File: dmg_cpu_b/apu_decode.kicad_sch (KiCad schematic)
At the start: 67 parts

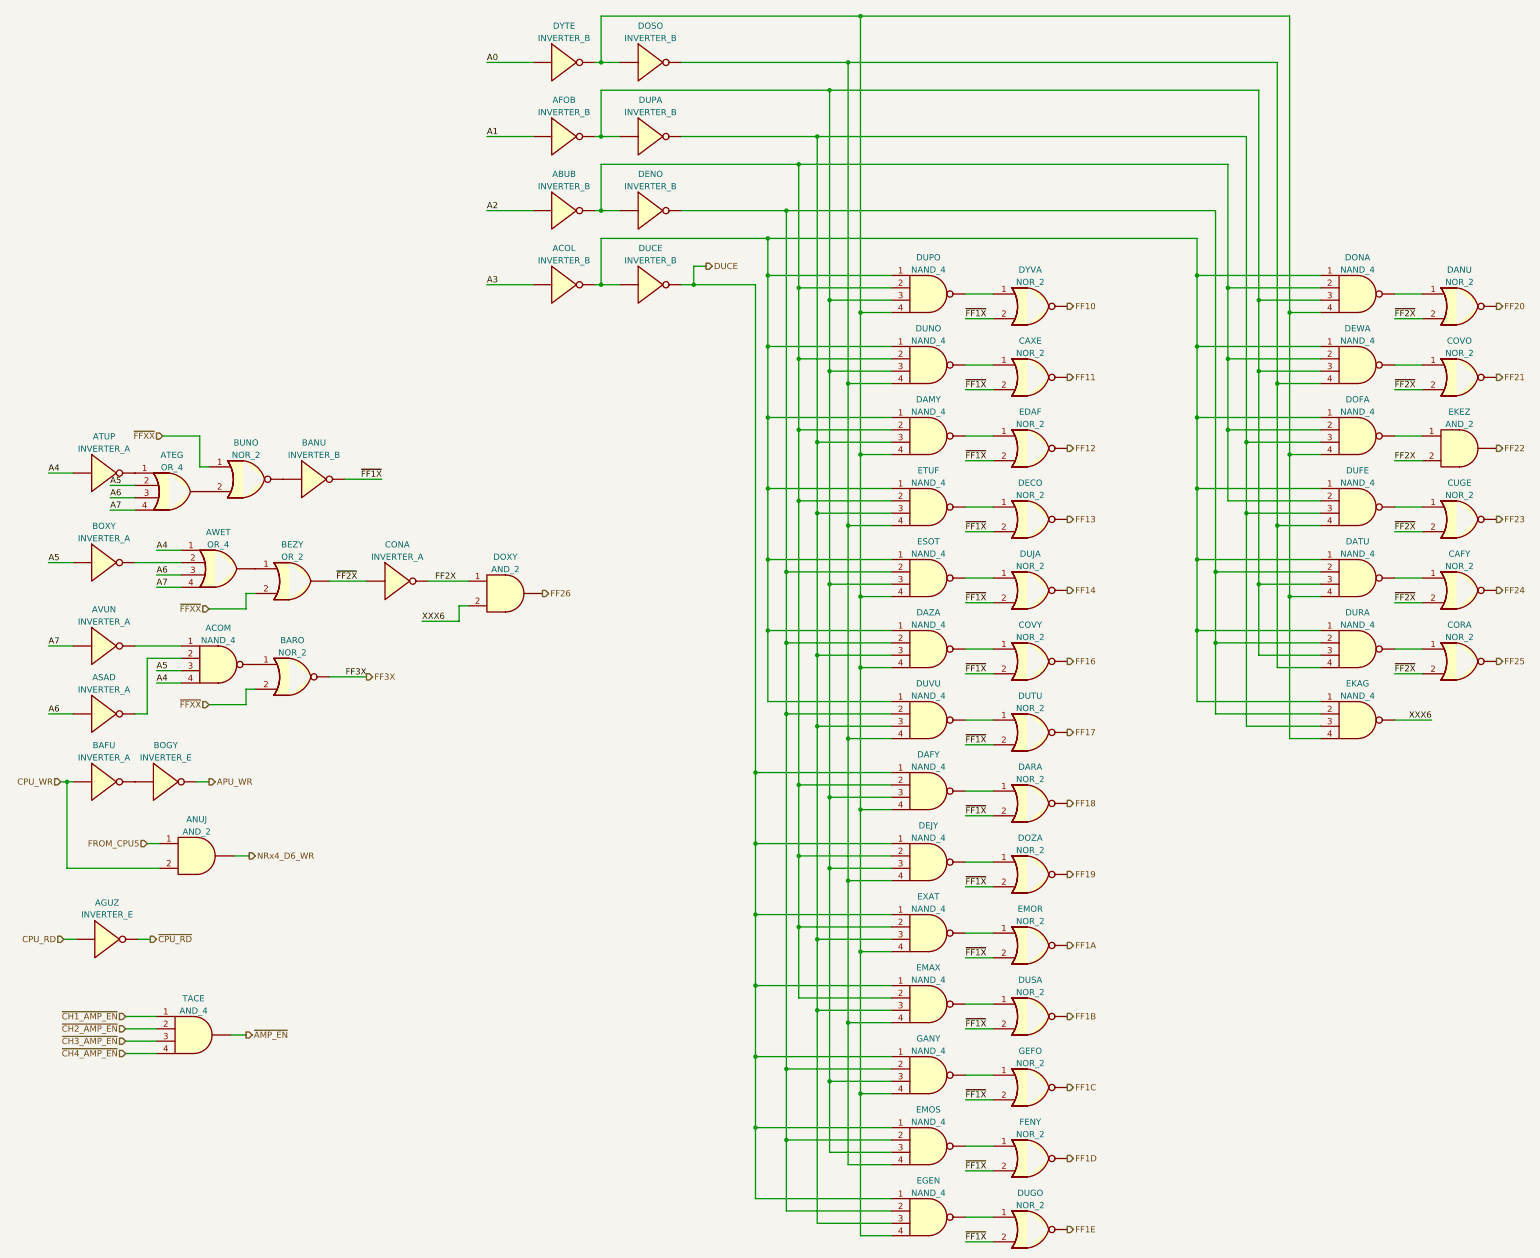
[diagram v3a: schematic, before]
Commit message: Fixes made from issues, channel 4 sheet aded and tidy up of hierarchical APU sheet. Small fixes done here and there when doing ERC.
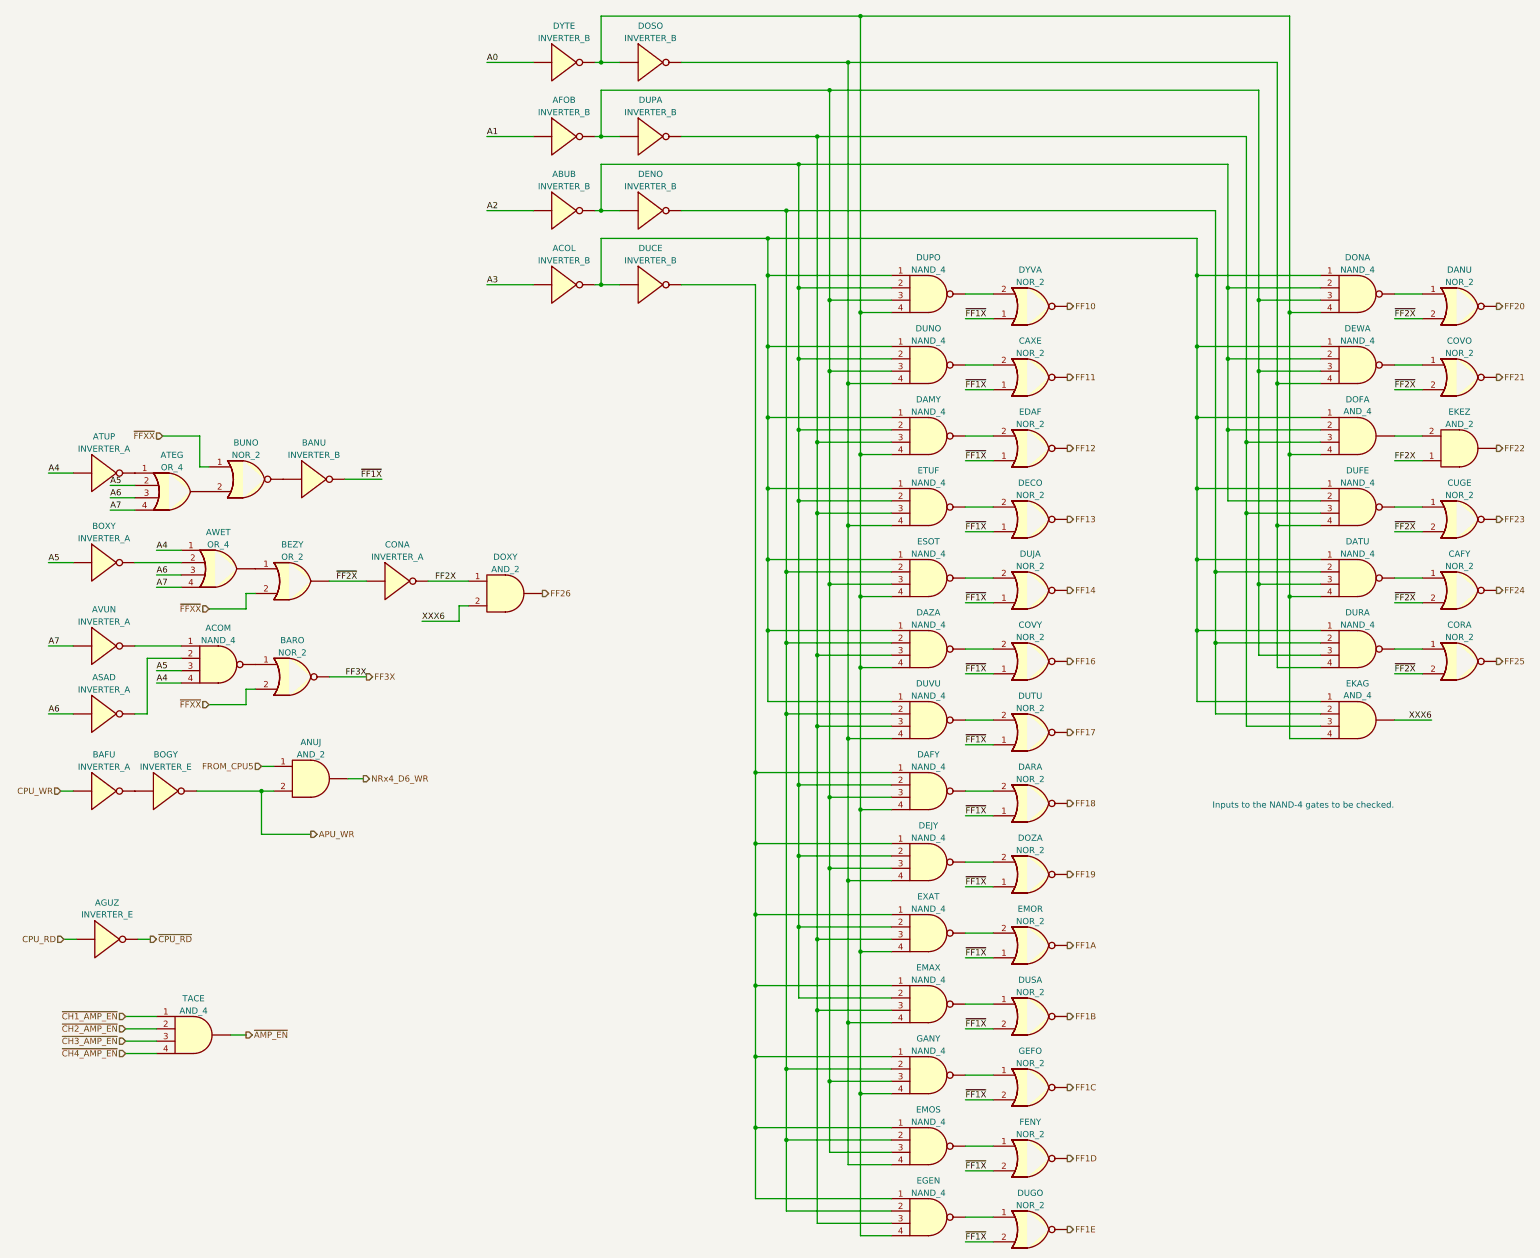
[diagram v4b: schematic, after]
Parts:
- DOFA, EKAG: value NAND_4 -> AND_4; symbol DMG_CPU_Cells:NAND_4 -> DMG_CPU_Cells:AND_4
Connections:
- net APU_WR: now also ANUJ.2
- net CPU_WR: no longer ANUJ.2
- net FF2X: now also EKEZ.1; no longer EKEZ.2
- net ~{FF1X}: now also CAXE.1, COVY.1, DARA.1, DECO.1, DOZA.1, DUJA.1, DUTU.1, DYVA.1, EDAF.1, EMOR.1; no longer CAXE.2, COVY.2, DARA.2, DECO.2, DOZA.2, DUJA.2, DUTU.2, DYVA.2, EDAF.2, EMOR.2
- net at DUVU.5: now also DUTU.2; no longer DUTU.1
- net at DUPO.5: now also DYVA.2; no longer DYVA.1
- net at ETUF.5: now also DECO.2; no longer DECO.1
- net at DAFY.5: now also DARA.2; no longer DARA.1
- net at DAZA.5: now also COVY.2; no longer COVY.1
- net at DOFA.5: now also EKEZ.2; no longer EKEZ.1
- net at EXAT.5: now also EMOR.2; no longer EMOR.1
- net at DAMY.5: now also EDAF.2; no longer EDAF.1
- net at DEJY.5: now also DOZA.2; no longer DOZA.1
- net at DUNO.5: now also CAXE.2; no longer CAXE.1
- net at ESOT.5: now also DUJA.2; no longer DUJA.1
- net DUCE: no longer names the net of DAFY.1, DEJY.1, DUCE.2, EGEN.1, EMAX.1, EMOS.1, EXAT.1, GANY.1
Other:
- note added: "Inputs to the NAND-4 gates to be checked."
- moved on the sheet: ANUJ, BAFU, BOGY

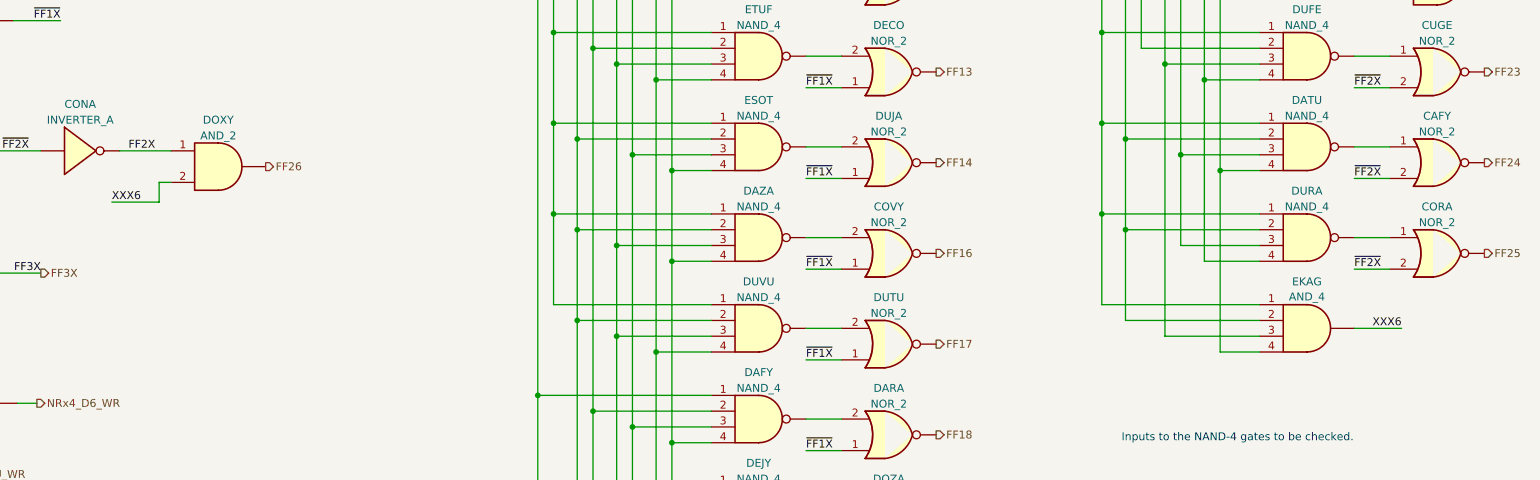
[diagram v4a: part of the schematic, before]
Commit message: DOXY moved for consistency.
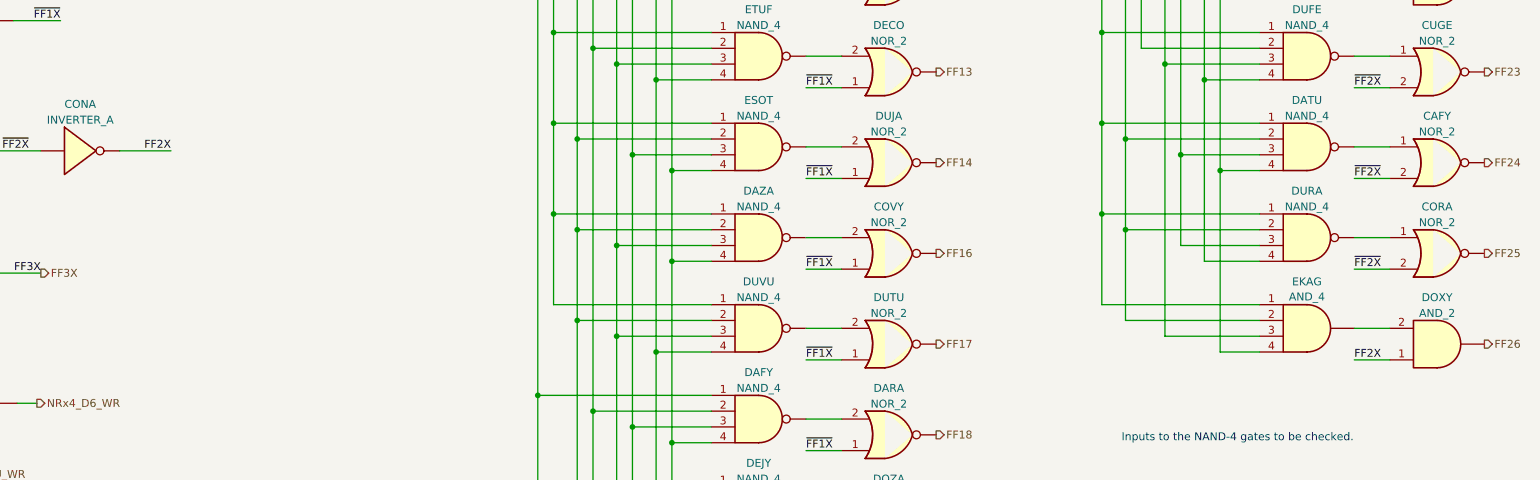
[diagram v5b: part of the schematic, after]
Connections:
- net XXX6: no longer names the net of DOXY.2, EKAG.5
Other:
- moved on the sheet: DOXY
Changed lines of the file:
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@@
     (stroke (width 0) (type default) (color 0 0 0 0))
   )
-  (wire (pts (xy 330.835 166.37) (xy 338.455 166.37))
+  (wire (pts (xy 330.835 166.37) (xy 336.55 166.37))
     (stroke (width 0) (type default) (color 0 0 0 0))
   )
@@
     (stroke (width 0) (type default) (color 0 0 0 0))
   )
-  (wire (pts (xy 130.81 146.05) (xy 138.43 146.05))
-    (stroke (width 0) (type default) (color 0 0 0 0))
-  )
   (wire (pts (xy 208.28 52.07) (xy 208.28 77.47))
     (stroke (width 0) (type default) (color 0 0 0 0))
@@
     (stroke (width 0) (type default) (color 0 0 0 0))
   )
-  (wire (pts (xy 138.43 142.875) (xy 138.43 146.05))
-    (stroke (width 0) (type default) (color 0 0 0 0))
-  )
   (wire (pts (xy 140.335 137.795) (xy 132.08 137.795))
     (stroke (width 0) (type default) (color 0 0 0 0))
   )
-  (wire (pts (xy 140.335 142.875) (xy 138.43 142.875))
-    (stroke (width 0) (type default) (color 0 0 0 0))
-  )
   (wire (pts (xy 166.37 76.835) (xy 167.64 76.835))
     (stroke (width 0) (type default) (color 0 0 0 0))
@@
   )
   (wire (pts (xy 300.355 123.825) (xy 315.595 123.825))
+    (stroke (width 0) (type default) (color 0 0 0 0))
+  )
+  (wire (pts (xy 330.835 171.45) (xy 336.55 171.45))
     (stroke (width 0) (type default) (color 0 0 0 0))
   )
@@
     (effects (font (size 1.27 1.27)) (justify left bottom))
   )
+  (label "FF2X" (at 330.835 171.45 0)
+    (effects (font (size 1.27 1.27)) (justify left bottom))
+  )
   (label "~{FF2X}" (at 330.835 127.635 0)
     (effects (font (size 1.27 1.27)) (justify left bottom))
@@
     (effects (font (size 1.27 1.27)) (justify left bottom))
   )
-  (label "FF2X" (at 137.795 137.795 180)
+  (label "FF2X" (at 140.335 137.795 180)
     (effects (font (size 1.27 1.27)) (justify right bottom))
   )
@@
     (effects (font (size 1.27 1.27)) (justify right bottom))
   )
-  (label "XXX6" (at 338.455 166.37 180)
-    (effects (font (size 1.27 1.27)) (justify right bottom))
-  )
   (label "A5" (at 53.975 133.985 0)
     (effects (font (size 1.27 1.27)) (justify left bottom))
@@
     (effects (font (size 1.27 1.27)) (justify left bottom))
   )
-  (label "XXX6" (at 130.81 146.05 0)
-    (effects (font (size 1.27 1.27)) (justify left bottom))
-  )
   (label "A7" (at 66.675 123.19 0)
     (effects (font (size 1.27 1.27)) (justify left bottom))
@@
     (effects (font (size 1.27 1.27)) (justify left))
   )
-  (hierarchical_label "FF26" (shape output) (at 155.575 140.335 0)
+  (hierarchical_label "FF26" (shape output) (at 351.79 168.91 0)
     (effects (font (size 1.27 1.27)) (justify left))
   )
@@
     (pin "5")
   )
-  (symbol (lib_id "DMG_CPU_Cells:AND_2") (at 147.955 140.335 0) (unit 1)
+  (symbol (lib_id "DMG_CPU_Cells:AND_2") (at 344.17 168.91 0) (mirror x) (unit 1)
     (in_bom yes) (on_board yes) (fields_autoplaced)
-    (property "Reference" "DOXY" (id 0) (at 147.955 132.8252 0))
-    (property "Value" "AND_2" (id 1) (at 147.955 135.3621 0))
-    (property "Footprint" "" (id 2) (at 147.955 140.335 0)
+    (property "Reference" "DOXY" (id 0) (at 344.17 161.4002 0))
+    (property "Value" "AND_2" (id 1) (at 344.17 163.9371 0))
+    (property "Footprint" "" (id 2) (at 344.17 168.91 0)
       (effects (font (size 1.27 1.27)) hide)
     )
-    (property "Datasheet" "http://iceboy.a-singer.de/doc/dmg_cells.html#and2" (id 3) (at 147.955 147.955 0)
+    (property "Datasheet" "http://iceboy.a-singer.de/doc/dmg_cells.html#and2" (id 3) (at 344.17 161.29 0)
       (effects (font (size 1.27 1.27)) hide)
     )

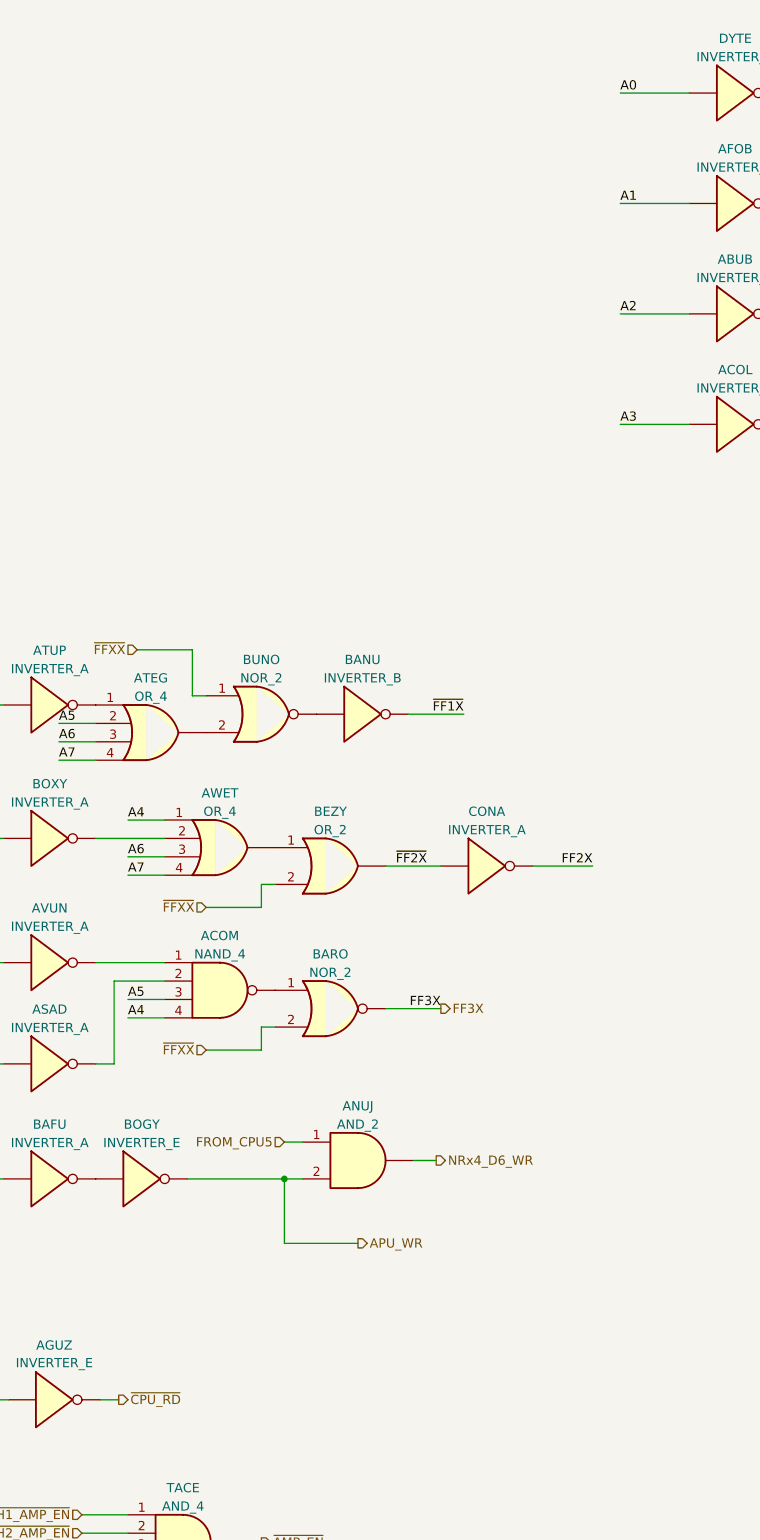
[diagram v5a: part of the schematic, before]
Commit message: Fixes made based on raised issues. PPU decode page added as draft level.
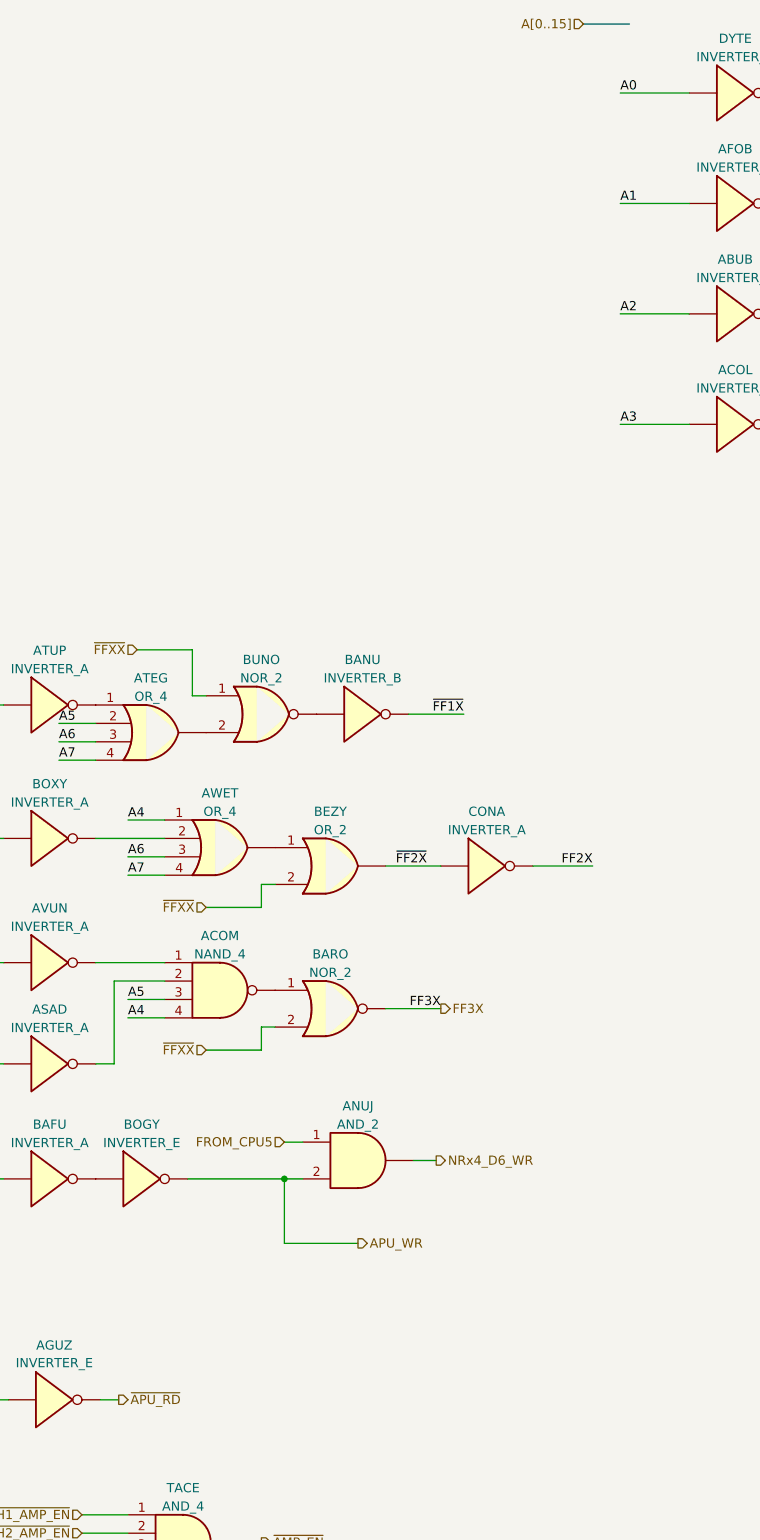
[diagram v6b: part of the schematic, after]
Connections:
- net ~{CPU_RD} renamed ~{APU_RD}
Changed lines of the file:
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@@
+    (stroke (width 0) (type default) (color 0 0 0 0))
+  )
+  (bus (pts (xy 139.065 21.59) (xy 145.415 21.59))
     (stroke (width 0) (type default) (color 0 0 0 0))
   )
@@
     (effects (font (size 1.27 1.27)) (justify left))
   )
-  (hierarchical_label "~{CPU_RD}" (shape output) (at 74.93 211.455 0)
+  (hierarchical_label "~{APU_RD}" (shape output) (at 74.93 211.455 0)
     (effects (font (size 1.27 1.27)) (justify left))
   )
@@
     (effects (font (size 1.27 1.27)) (justify left))
   )
+  (hierarchical_label "A[0..15]" (shape input) (at 139.065 21.59 180)
+    (effects (font (size 1.27 1.27)) (justify right))
+  )
   (hierarchical_label "~{FFXX}" (shape input) (at 77.47 107.95 180)
